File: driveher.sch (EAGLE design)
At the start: 21 parts, among them Q1 PSMN, Q2 PSMN

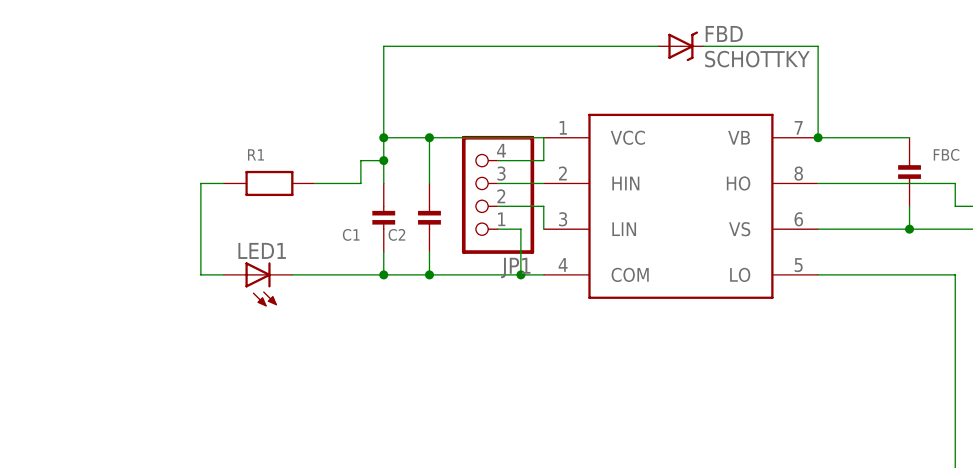
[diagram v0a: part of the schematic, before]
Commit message: fixed ir25606 / '67 routing, beefed up trace b/t high side source & output, added input protect resistors
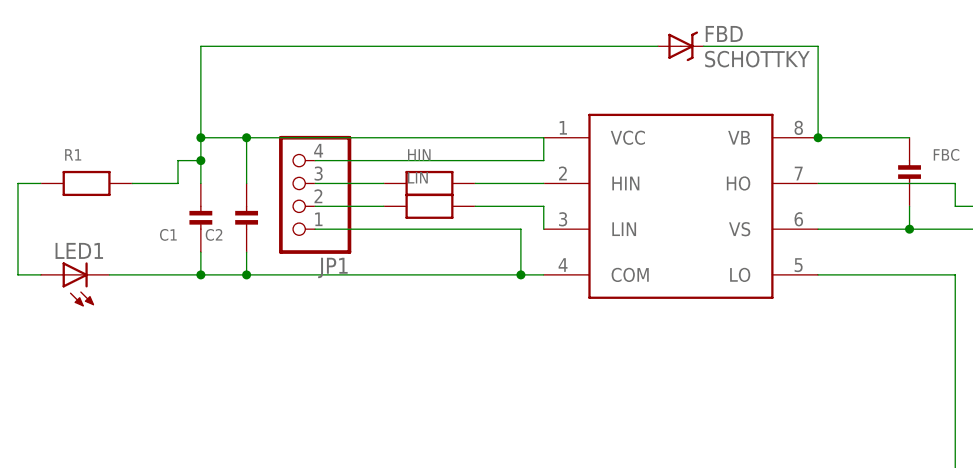
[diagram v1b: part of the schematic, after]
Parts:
- added HIN, LIN: (no value), nonolith:RESISTOR0603
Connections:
- removed net HIN: JP1.3, U$1.HIN
- removed net LIN: JP1.2, U$1.LIN
- new net HIN-P: HIN.2, U$1.HIN
- new net LIN-P: LIN.2, U$1.LIN
- new net N$3: HIN.1, JP1.3
- new net N$4: JP1.2, LIN.1
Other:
- moved on the sheet: C1, C2, JP1, LED1, R1
